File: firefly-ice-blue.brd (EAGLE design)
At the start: 34 x 33.5 mm, 119 parts, among them J1 USB-5PINMOLEX-47346, J2 CON-6SOCKET, U1 EFM32LG330F256, U10 STM6519, U11 TPS782XX, U12 TPS6208X, U13 NX3L1T53, U14 FDFMA2P029Z, U16 MEMORY-SPIWLBGA-8, U17 ADP151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

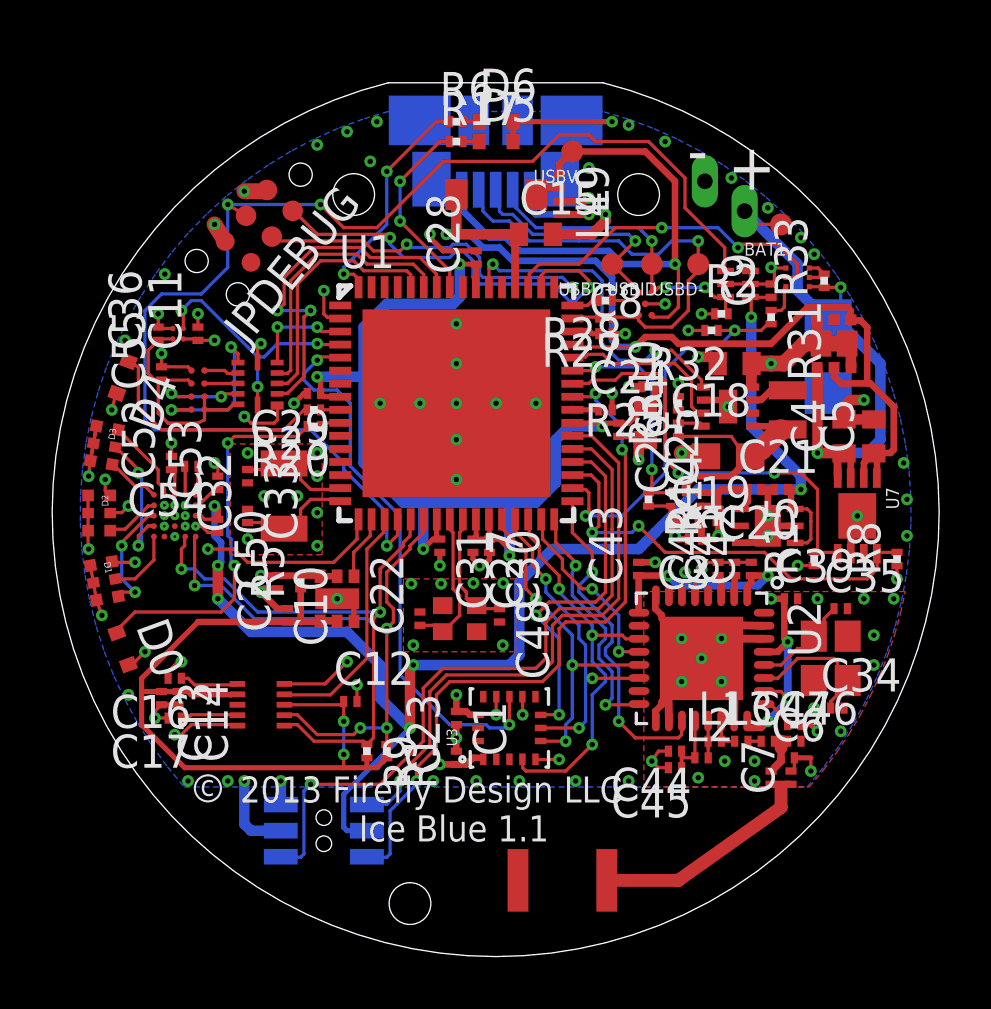
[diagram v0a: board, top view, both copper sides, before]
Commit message: switch to splashproof USB connector; fix voltage translator connections (swap A and B sides); DFM improvements
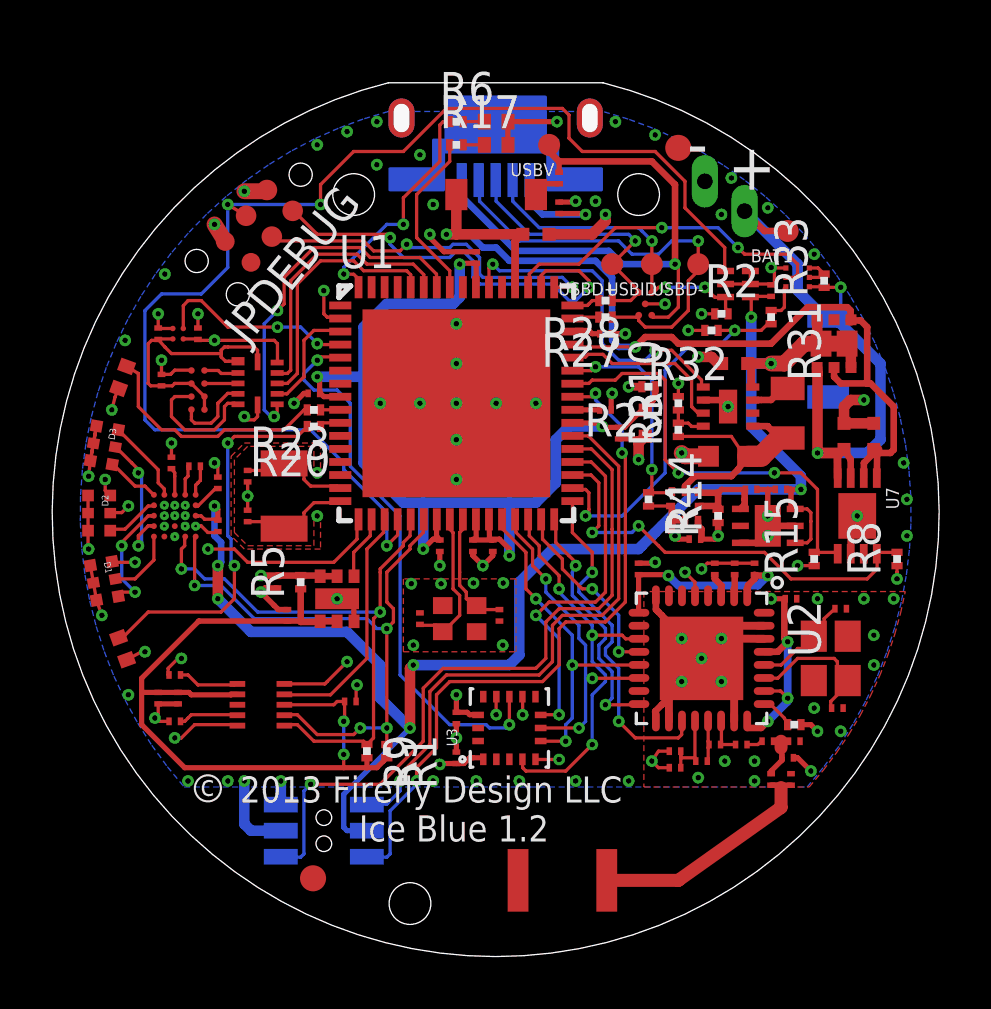
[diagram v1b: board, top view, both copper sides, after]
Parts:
- J1: value USB-5PINMOLEX-47346 -> USB-5PINZX62WD1-B-5PC; device firefly:MOLEX-47346 -> firefly:ZX62WD1-B-5PC
- moved J1 4.79 mm to (17.0, 33.5)
- moved USBV 0.92 mm to (19.1, 31.1)
- moved BAT1 0.36 mm to (28.2, 27.8)
- moved C55 0.25 mm to (4.19, 22.1)
- moved C26 0.13 mm to (21.7, 20.1)
- moved C40 0.13 mm to (25.4, 14.9)
- moved D5 0.13 mm to (17.0, 31.1)
- moved R17 0.13 mm to (15.5, 31.1)
- moved C16 0.13 mm to (4.70, 10.8)
- moved C17 0.13 mm to (4.70, 9.02)
- moved C54 0.13 mm to (5.46, 18.8)
- moved L1 0.13 mm to (25.4, 8.13)
- moved L3 0.13 mm to (26.4, 8.13)
- moved C13 0.13 mm to (4.06, 9.91)
- moved L2 0.13 mm to (24.9, 7.49)
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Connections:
- removed net N$14: U16.C1, U18.9
- removed net N$18: U16.D1, U18.8
- new net SPI0_CLK: U16.C1, U18.3
- new net SPI0_MOSI: U16.D1, U18.2
- net MEM_CSN: now also U18.8; no longer U18.5
- net SPI0_CSN: now also U18.4; no longer U18.7
- net SPI0_MISO: now also U18.5; no longer U18.10
- net SPI0_V+: now also U18.1, U18.12; no longer U18.11
- net US0_CLK: now also U18.9; no longer U18.3
- net US0_MISO: now also U18.7; no longer U18.2
- net US0_MOSI: now also U18.10; no longer U18.4
- net US0_PWR: no longer U18.12
- net VCC: now also U18.11; no longer U18.1
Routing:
- net SPI0_CSN: track 6.21 -> 3.01 mm, vias 2 -> 0
- net US0_PWR: track 9.92 -> 7.67 mm, vias 3 -> 2
- net GND: track 88.3 -> 90.1 mm, vias 116 -> 113
- net SPI0_V+: track 9.38 -> 11.1 mm
- net SPI0_MISO: track 3.41 -> 4.95 mm, vias 2 -> 0
- net SPI0_MOSI: track 0.00 -> 1.34 mm
- net N$18: track 1.34 -> 0.00 mm
- net SPI0_CLK: track 0.00 -> 1.29 mm
- net N$14: track 1.29 -> 0.00 mm
- net NRESET: track 48.9 -> 49.9 mm
- net LED5: track 7.38 -> 6.51 mm, vias 2 -> 0
- net N$42: track 40.8 -> 41.6 mm
- net USB_VBUS: track 40.6 -> 41.2 mm
- net MEM_CSN: track 3.84 -> 4.25 mm, vias 2 -> 0
- net VCC: track 40.2 -> 40.0 mm, vias 20 -> 19
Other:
- board text added: "Ice Blue 1.2"
- board text added: "J1"
- board text added: "PTH"
- board text removed: "Ice Blue 1.1"

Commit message: fix power/ground short in USB connector mounting posts; fix MOSI/MISO to memory and add chip select pullup
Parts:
- added R7: 100k, firefly:R0201
- moved C52 0.13 mm to (4.57, 18.8), turned to 180 degrees
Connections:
- net SPI0_CSN: now also R7.2
- net SPI0_V+: now also R7.1
- net US0_MISO: now also U1.59; no longer U1.58
- net US0_MOSI: now also U1.58; no longer U1.59
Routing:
- net SPI0_CSN: track 3.01 -> 5.51 mm, vias 0 -> 2
- net NRESET: track 49.9 -> 48.6 mm
- net US0_MISO: track 13.6 -> 12.6 mm
- net SPI0_MISO: track 4.95 -> 5.92 mm
- net N$15: track 9.16 -> 10.1 mm
- net US0_MOSI: track 10.4 -> 11.3 mm
- net SPI0_V+: track 11.1 -> 11.7 mm
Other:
- board text added: "Ice Blue 1.3"
- board text removed: "Ice Blue 1.2"
